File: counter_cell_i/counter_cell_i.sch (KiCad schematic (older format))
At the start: 1 part, among them P1 DIN_41612_128P

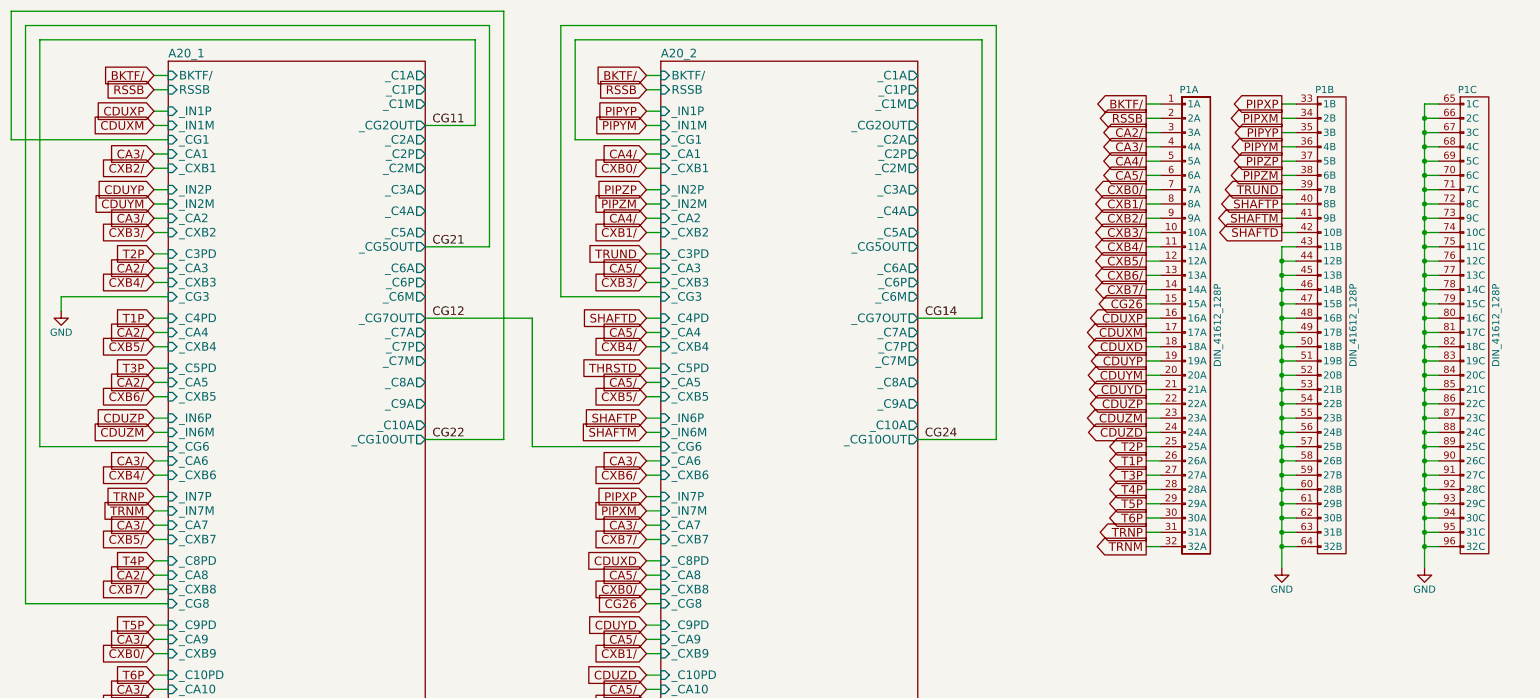
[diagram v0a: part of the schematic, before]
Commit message: Tied in modules 20 and 21
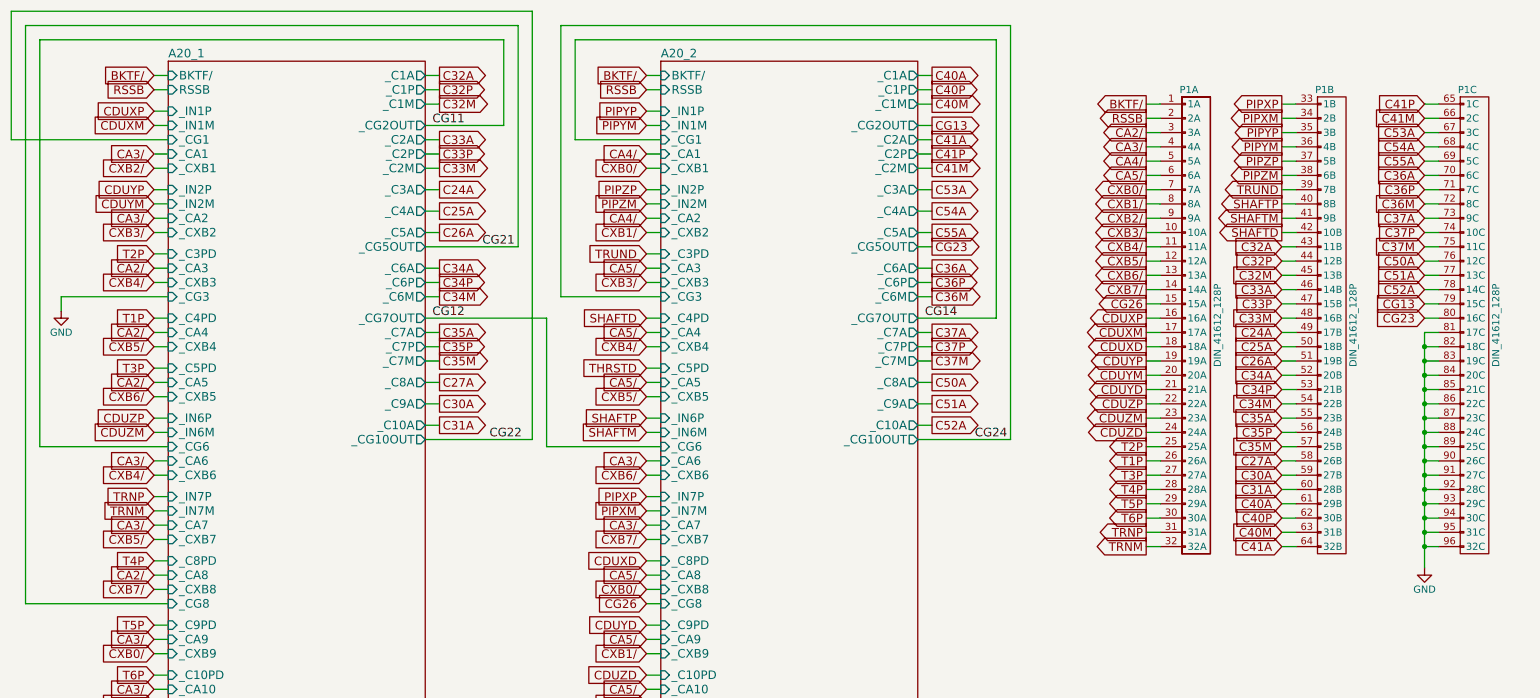
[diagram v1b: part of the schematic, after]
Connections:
- net GND: no longer P1.43 (11B), P1.44 (12B), P1.45 (13B), P1.46 (14B), P1.47 (15B), P1.48 (16B), P1.49 (17B), P1.50 (18B), P1.51 (19B), P1.52 (20B), P1.53 (21B), P1.54 (22B), P1.55 (23B), P1.56 (24B), P1.57 (25B), P1.58 (26B), P1.59 (27B), P1.60 (28B), P1.61 (29B), P1.62 (30B), P1.63 (31B), P1.64 (32B), P1.65 (1C), P1.66 (2C), P1.67 (3C), P1.68 (4C), P1.69 (5C), P1.70 (6C), P1.71 (7C), P1.72 (8C), P1.73 (9C), P1.74 (10C), P1.75 (11C), P1.76 (12C), P1.77 (13C), P1.78 (14C), P1.79 (15C), P1.80 (16C)
- new net C24A: P1.49 (17B)
- new net C25A: P1.50 (18B)
- new net C26A: P1.51 (19B)
- new net C27A: P1.58 (26B)
- new net C30A: P1.59 (27B)
- new net C31A: P1.60 (28B)
- new net C32A: P1.43 (11B)
- new net C32M: P1.45 (13B)
- new net C32P: P1.44 (12B)
- new net C33A: P1.46 (14B)
- new net C33M: P1.48 (16B)
- new net C33P: P1.47 (15B)
- new net C34A: P1.52 (20B)
- new net C34M: P1.54 (22B)
- new net C34P: P1.53 (21B)
- new net C35A: P1.55 (23B)
- new net C35M: P1.57 (25B)
- new net C35P: P1.56 (24B)
- new net C36A: P1.70 (6C)
- new net C36M: P1.72 (8C)
- new net C36P: P1.71 (7C)
- new net C37A: P1.73 (9C)
- new net C37M: P1.75 (11C)
- new net C37P: P1.74 (10C)
- new net C40A: P1.61 (29B)
- new net C40M: P1.63 (31B)
- new net C40P: P1.62 (30B)
- new net C41A: P1.64 (32B)
- new net C41M: P1.66 (2C)
- new net C41P: P1.65 (1C)
- new net C50A: P1.76 (12C)
- new net C51A: P1.77 (13C)
- new net C52A: P1.78 (14C)
- new net C53A: P1.67 (3C)
- new net C54A: P1.68 (4C)
- new net C55A: P1.69 (5C)
- new net CG13: P1.79 (15C)
- new net CG23: P1.80 (16C)

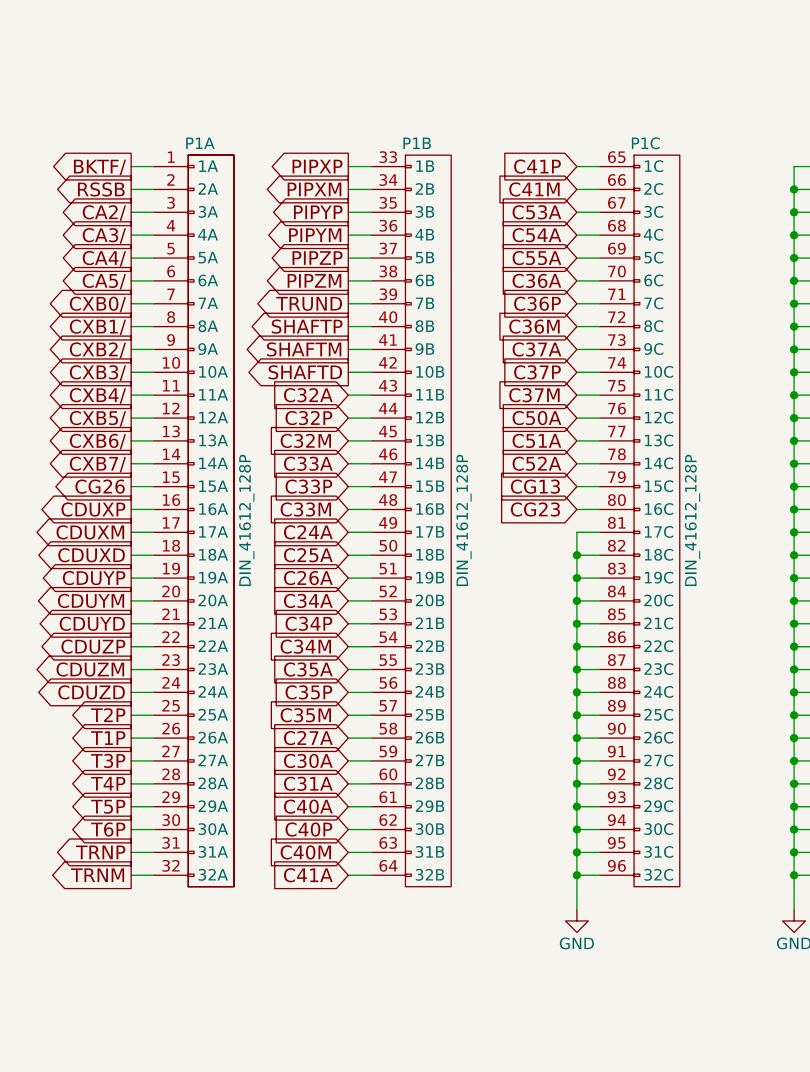
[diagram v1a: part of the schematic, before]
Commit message: Added and tied in the Alarms module.
I've placed page 2 of Counter Cell 2 here as page 2 of alarms. It didn't
fit in the counter cells, despite producing a few counter-related
signals -- and it mostly handles monitor stuff, which is a good fit for
what's going on here. As part of this I modernized the timer and scaler
connectors.

There seems to be lots of oscillations in the the simulation. Initial
conditions to correct those to follow.
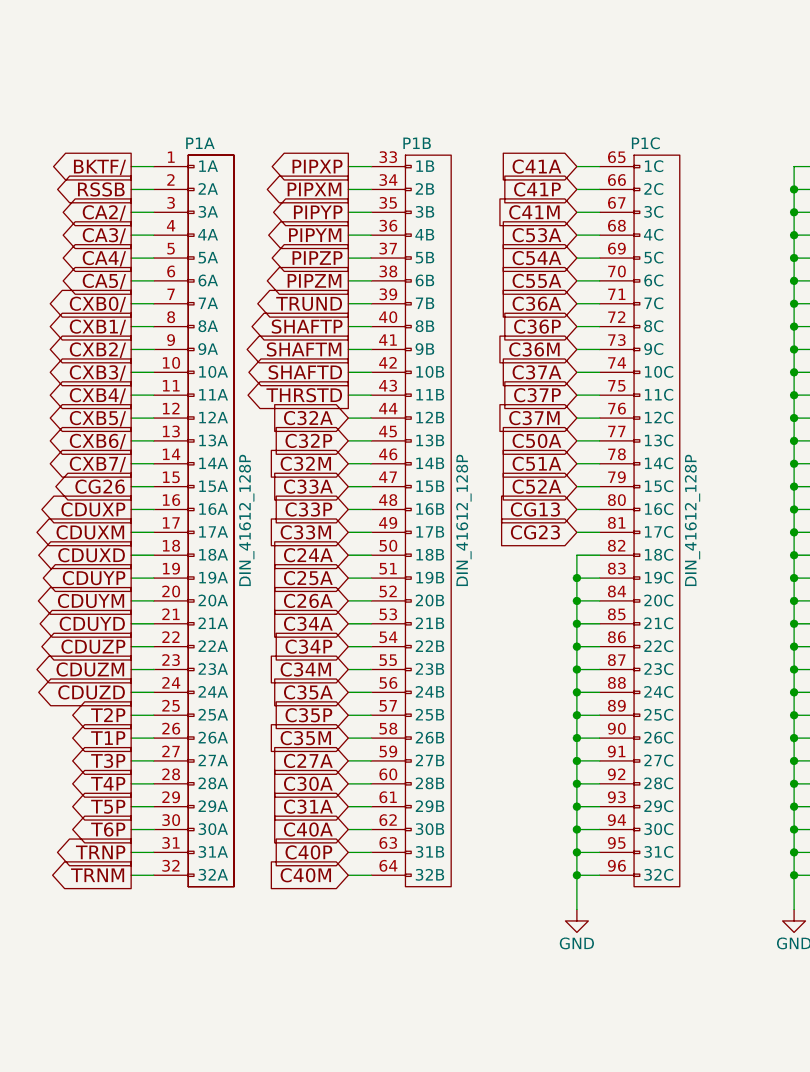
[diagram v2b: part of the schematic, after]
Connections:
- net C24A: now also P1.50 (18B); no longer P1.49 (17B)
- net C25A: now also P1.51 (19B); no longer P1.50 (18B)
- net C26A: now also P1.52 (20B); no longer P1.51 (19B)
- net C27A: now also P1.59 (27B); no longer P1.58 (26B)
- net C30A: now also P1.60 (28B); no longer P1.59 (27B)
- net C31A: now also P1.61 (29B); no longer P1.60 (28B)
- net C32A: now also P1.44 (12B); no longer P1.43 (11B)
- net C32M: now also P1.46 (14B); no longer P1.45 (13B)
- net C32P: now also P1.45 (13B); no longer P1.44 (12B)
- net C33A: now also P1.47 (15B); no longer P1.46 (14B)
- net C33M: now also P1.49 (17B); no longer P1.48 (16B)
- net C33P: now also P1.48 (16B); no longer P1.47 (15B)
- net C34A: now also P1.53 (21B); no longer P1.52 (20B)
- net C34M: now also P1.55 (23B); no longer P1.54 (22B)
- net C34P: now also P1.54 (22B); no longer P1.53 (21B)
- net C35A: now also P1.56 (24B); no longer P1.55 (23B)
- net C35M: now also P1.58 (26B); no longer P1.57 (25B)
- net C35P: now also P1.57 (25B); no longer P1.56 (24B)
- net C36A: now also P1.71 (7C); no longer P1.70 (6C)
- net C36M: now also P1.73 (9C); no longer P1.72 (8C)
- net C36P: now also P1.72 (8C); no longer P1.71 (7C)
- net C37A: now also P1.74 (10C); no longer P1.73 (9C)
- net C37M: now also P1.76 (12C); no longer P1.75 (11C)
- net C37P: now also P1.75 (11C); no longer P1.74 (10C)
- net C40A: now also P1.62 (30B); no longer P1.61 (29B)
- net C40M: now also P1.64 (32B); no longer P1.63 (31B)
- net C40P: now also P1.63 (31B); no longer P1.62 (30B)
- net C41A: now also P1.65 (1C); no longer P1.64 (32B)
- net C41M: now also P1.67 (3C); no longer P1.66 (2C)
- net C41P: now also P1.66 (2C); no longer P1.65 (1C)
- net C50A: now also P1.77 (13C); no longer P1.76 (12C)
- net C51A: now also P1.78 (14C); no longer P1.77 (13C)
- net C52A: now also P1.79 (15C); no longer P1.78 (14C)
- net C53A: now also P1.68 (4C); no longer P1.67 (3C)
- net C54A: now also P1.69 (5C); no longer P1.68 (4C)
- net C55A: now also P1.70 (6C); no longer P1.69 (5C)
- net CG13: now also P1.80 (16C); no longer P1.79 (15C)
- net CG23: now also P1.81 (17C); no longer P1.80 (16C)
- net GND: no longer P1.81 (17C)
- net THRSTD: now also P1.43 (11B)
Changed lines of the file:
@@
 Wire Wire Line
 	3750 1200 3650 1200
-Text GLabel 9650 2200 0    60   Input ~ 0
+Text GLabel 9650 2300 0    60   Input ~ 0
 C32A
-Wire Wire Line
-	9650 2200 9750 2200
-Text GLabel 9650 2300 0    60   Input ~ 0
-C32P
 Wire Wire Line
 	9650 2300 9750 2300
 Text GLabel 9650 2400 0    60   Input ~ 0
+C32P
+Wire Wire Line
+	9650 2400 9750 2400
+Text GLabel 9650 2500 0    60   Input ~ 0
 C32M
 Wire Wire Line
-	9650 2400 9750 2400
+	9650 2500 9750 2500
 Text GLabel 3750 1450 2    60   Output ~ 0
 C33A
@@
 Wire Wire Line
 	3750 1650 3650 1650
-Text GLabel 9650 2500 0    60   Input ~ 0
+Text GLabel 9650 2600 0    60   Input ~ 0
 C33A
-Wire Wire Line
-	9650 2500 9750 2500
-Text GLabel 9650 2600 0    60   Input ~ 0
-C33P
 Wire Wire Line
 	9650 2600 9750 2600
 Text GLabel 9650 2700 0    60   Input ~ 0
+C33P
+Wire Wire Line
+	9650 2700 9750 2700
+Text GLabel 9650 2800 0    60   Input ~ 0
 C33M
 Wire Wire Line
-	9650 2700 9750 2700
+	9650 2800 9750 2800
 Text GLabel 3750 1800 2    60   Output ~ 0
 C24A
@@
 Wire Wire Line
 	3750 2100 3650 2100
-Text GLabel 9650 2800 0    60   Input ~ 0
+Text GLabel 9650 2900 0    60   Input ~ 0
 C24A
-Wire Wire Line
-	9650 2800 9750 2800
-Text GLabel 9650 2900 0    60   Input ~ 0
-C25A
 Wire Wire Line
 	9650 2900 9750 2900
 Text GLabel 9650 3000 0    60   Input ~ 0
+C25A
+Wire Wire Line
+	9650 3000 9750 3000
+Text GLabel 9650 3100 0    60   Input ~ 0
 C26A
 Wire Wire Line
-	9650 3000 9750 3000
+	9650 3100 9750 3100
 Text GLabel 3750 2350 2    60   Output ~ 0
 C34A
@@
 Wire Wire Line
 	3750 2550 3650 2550
-Text GLabel 9650 3100 0    60   Input ~ 0
+Text GLabel 9650 3200 0    60   Input ~ 0
 C34A
-Wire Wire Line
-	9650 3100 9750 3100
-Text GLabel 9650 3200 0    60   Input ~ 0
-C34P
 Wire Wire Line
 	9650 3200 9750 3200
 Text GLabel 9650 3300 0    60   Input ~ 0
+C34P
+Wire Wire Line
+	9650 3300 9750 3300
+Text GLabel 9650 3400 0    60   Input ~ 0
 C34M
 Wire Wire Line
-	9650 3300 9750 3300
+	9650 3400 9750 3400
 Text GLabel 3750 2800 2    60   Output ~ 0
 C35A
@@
 Wire Wire Line
 	3750 3450 3650 3450
-Text GLabel 9650 3700 0    60   Input ~ 0
+Text GLabel 9650 3800 0    60   Input ~ 0
 C27A
-Wire Wire Line
-	9650 3700 9750 3700
-Text GLabel 9650 3800 0    60   Input ~ 0
-C30A
 Wire Wire Line
 	9650 3800 9750 3800
 Text GLabel 9650 3900 0    60   Input ~ 0
+C30A
+Wire Wire Line
+	9650 3900 9750 3900
+Text GLabel 9650 4000 0    60   Input ~ 0
 C31A
 Wire Wire Line
-	9650 3900 9750 3900
-Text GLabel 9650 3400 0    60   Input ~ 0
+	9650 4000 9750 4000
+Text GLabel 9650 3500 0    60   Input ~ 0
 C35A
-Wire Wire Line
-	9650 3400 9750 3400
-Text GLabel 9650 3500 0    60   Input ~ 0
-C35P
 Wire Wire Line
 	9650 3500 9750 3500
 Text GLabel 9650 3600 0    60   Input ~ 0
+C35P
+Wire Wire Line
+	9650 3600 9750 3600
+Text GLabel 9650 3700 0    60   Input ~ 0
 C35M
 Wire Wire Line
-	9650 3600 9750 3600
+	9650 3700 9750 3700
 Text GLabel 7200 1000 2    60   Output ~ 0
 C40A
@@
 Wire Wire Line
 	7200 1200 7100 1200
-Text GLabel 9650 4000 0    60   Input ~ 0
+Text GLabel 9650 4100 0    60   Input ~ 0
 C40A
-Wire Wire Line
-	9650 4000 9750 4000
-Text GLabel 9650 4100 0    60   Input ~ 0
-C40P
 Wire Wire Line
 	9650 4100 9750 4100
 Text GLabel 9650 4200 0    60   Input ~ 0
+C40P
+Wire Wire Line
+	9650 4200 9750 4200
+Text GLabel 9650 4300 0    60   Input ~ 0
 C40M
 Wire Wire Line
-	9650 4200 9750 4200
+	9650 4300 9750 4300
 Text GLabel 7200 1450 2    60   Output ~ 0
 C41A
@@
 Wire Wire Line
 	7200 1650 7100 1650
-Text GLabel 9650 4300 0    60   Input ~ 0
+Text GLabel 10650 1200 0    60   Input ~ 0
 C41A
-Wire Wire Line
-	9650 4300 9750 4300
-Text GLabel 10650 1200 0    60   Input ~ 0
-C41P
 Wire Wire Line
 	10650 1200 10750 1200
 Text GLabel 10650 1300 0    60   Input ~ 0
+C41P
+Wire Wire Line
+	10650 1300 10750 1300
+Text GLabel 10650 1400 0    60   Input ~ 0
 C41M
 Wire Wire Line
-	10650 1300 10750 1300
+	10650 1400 10750 1400
 Text GLabel 7200 1800 2    60   Output ~ 0
 C53A
@@
 Wire Wire Line
 	7200 2100 7100 2100
-Text GLabel 10650 1400 0    60   Input ~ 0
+Text GLabel 10650 1500 0    60   Input ~ 0
 C53A
-Wire Wire Line
-	10650 1400 10750 1400
-Text GLabel 10650 1500 0    60   Input ~ 0
-C54A
 Wire Wire Line
 	10650 1500 10750 1500
 Text GLabel 10650 1600 0    60   Input ~ 0
+C54A
+Wire Wire Line
+	10650 1600 10750 1600
+Text GLabel 10650 1700 0    60   Input ~ 0
 C55A
 Wire Wire Line
-	10650 1600 10750 1600
+	10650 1700 10750 1700
 Text GLabel 7200 2350 2    60   Output ~ 0
 C36A
@@
 Wire Wire Line
 	7200 2550 7100 2550
-Text GLabel 10650 1700 0    60   Input ~ 0
+Text GLabel 10650 1800 0    60   Input ~ 0
 C36A
-Wire Wire Line
-	10650 1700 10750 1700
-Text GLabel 10650 1800 0    60   Input ~ 0
-C36P
 Wire Wire Line
 	10650 1800 10750 1800
 Text GLabel 10650 1900 0    60   Input ~ 0
+C36P
+Wire Wire Line
+	10650 1900 10750 1900
+Text GLabel 10650 2000 0    60   Input ~ 0
 C36M
 Wire Wire Line
-	10650 1900 10750 1900
+	10650 2000 10750 2000
 Text GLabel 7200 2800 2    60   Output ~ 0
 C37A
@@
 Wire Wire Line
 	7200 3000 7100 3000
-Text GLabel 10650 2000 0    60   Input ~ 0
+Text GLabel 10650 2100 0    60   Input ~ 0
 C37A
-Wire Wire Line
-	10650 2000 10750 2000
-Text GLabel 10650 2100 0    60   Input ~ 0
-C37P
 Wire Wire Line
 	10650 2100 10750 2100
 Text GLabel 10650 2200 0    60   Input ~ 0
+C37P
+Wire Wire Line
+	10650 2200 10750 2200
+Text GLabel 10650 2300 0    60   Input ~ 0
 C37M
 Wire Wire Line
-	10650 2200 10750 2200
+	10650 2300 10750 2300
 Text GLabel 7200 3150 2    60   Output ~ 0
 C50A
@@
 Wire Wire Line
 	7200 3450 7100 3450
-Text GLabel 10650 2300 0    60   Input ~ 0
+Text GLabel 10650 2400 0    60   Input ~ 0
 C50A
-Wire Wire Line
-	10650 2300 10750 2300
-Text GLabel 10650 2400 0    60   Input ~ 0
-C51A
 Wire Wire Line
 	10650 2400 10750 2400
 Text GLabel 10650 2500 0    60   Input ~ 0
+C51A
+Wire Wire Line
+	10650 2500 10750 2500
+Text GLabel 10650 2600 0    60   Input ~ 0
 C52A
 Wire Wire Line
-	10650 2500 10750 2500
-Wire Wire Line
-	10650 2800 10750 2800
+	10650 2600 10750 2600
 Wire Wire Line
 	10650 2900 10750 2900
-Connection ~ 10650 2900
 Wire Wire Line
 	10650 3000 10750 3000
@@
 Wire Wire Line
 	7200 2200 7100 2200
-Wire Wire Line
-	10650 2800 10650 4450
-Text GLabel 10650 2600 0    60   Input ~ 0
+Text GLabel 10650 2700 0    60   Input ~ 0
 CG13
 Wire Wire Line
-	10650 2600 10750 2600
-Text GLabel 10650 2700 0    60   Input ~ 0
+	10650 2700 10750 2700
+Text GLabel 10650 2800 0    60   Input ~ 0
 CG23
 Wire Wire Line
-	10650 2700 10750 2700
+	10650 2800 10750 2800
+Wire Wire Line
+	10650 2900 10650 4450
+Text GLabel 9650 2200 0    60   Output ~ 0
+THRSTD
+Wire Wire Line
+	9650 2200 9750 2200
 $EndSCHEMATC

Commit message: Power net updates for Counter Cell I+II and Inout V
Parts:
- added U20001, U20003, U20004, U20006, U20007, U20010, U20011, U20013, U20014, U20016, U20017, U20019, U20020, U20024, U20025, U20026, U20028, U20030, U20032, U20033, U20035, U20036, U20039, U20040, U20042, U20043, U20045, U20046, U20048, U20049, U20052, U20053, U20054: 74HC02, symbol 74HC02
- added U20002, U20023, U20031: 74HC04, symbol 74HC04
- added U20005, U20008, U20009, U20012, U20018, U20021, U20022, U20027, U20034, U20037, U20038, U20041, U20047, U20050, U20051, U20055: 74HC27, symbol 74HC27
- added U20015, U20029, U20044, U20056: 74HC4002, symbol 74HC4002
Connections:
- net labels added: +4VSW
- net labels removed: VCC
- wire segments 338 -> 350
